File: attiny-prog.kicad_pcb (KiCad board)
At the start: 2 copper layers, 53.3 x 53.1 mm, 9 parts, among them J1 SOIC16_clip

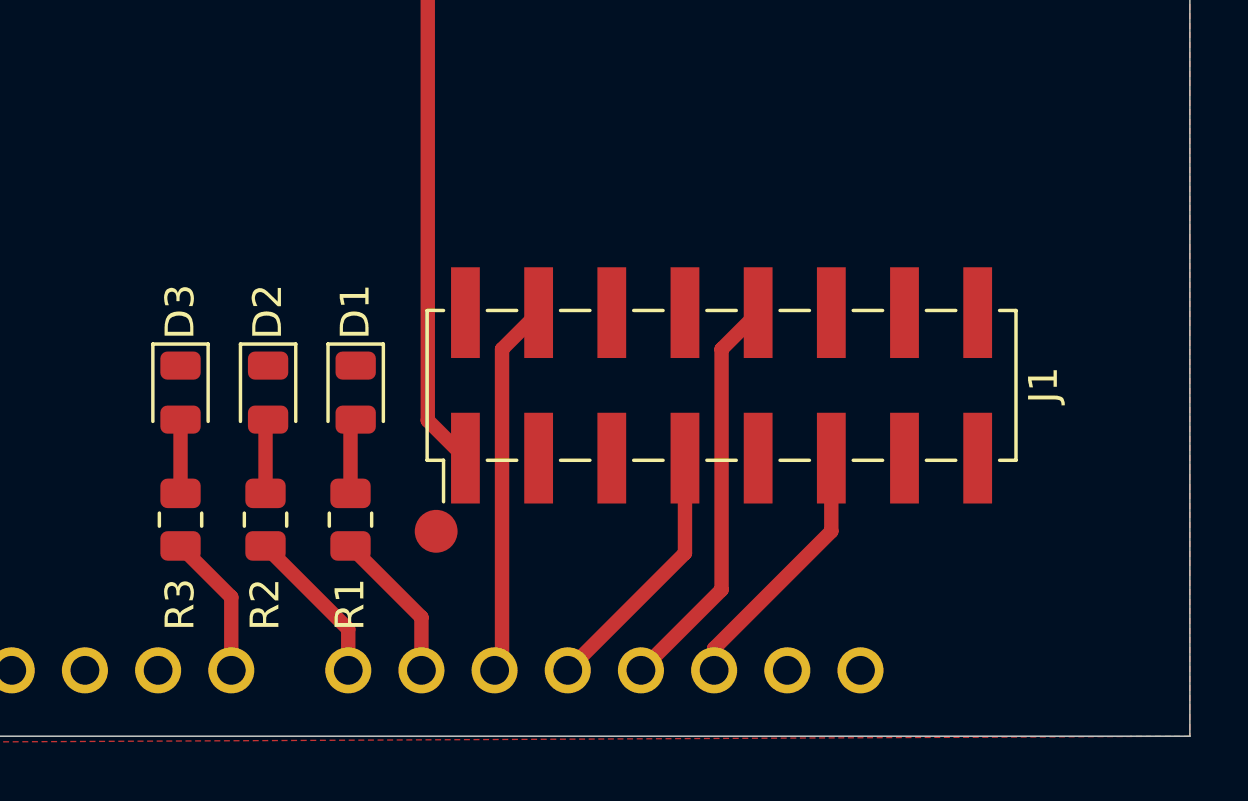
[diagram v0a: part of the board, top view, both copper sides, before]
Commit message: Second revision
* fixed SOIC_clip header pinout
* added reset capacitor value
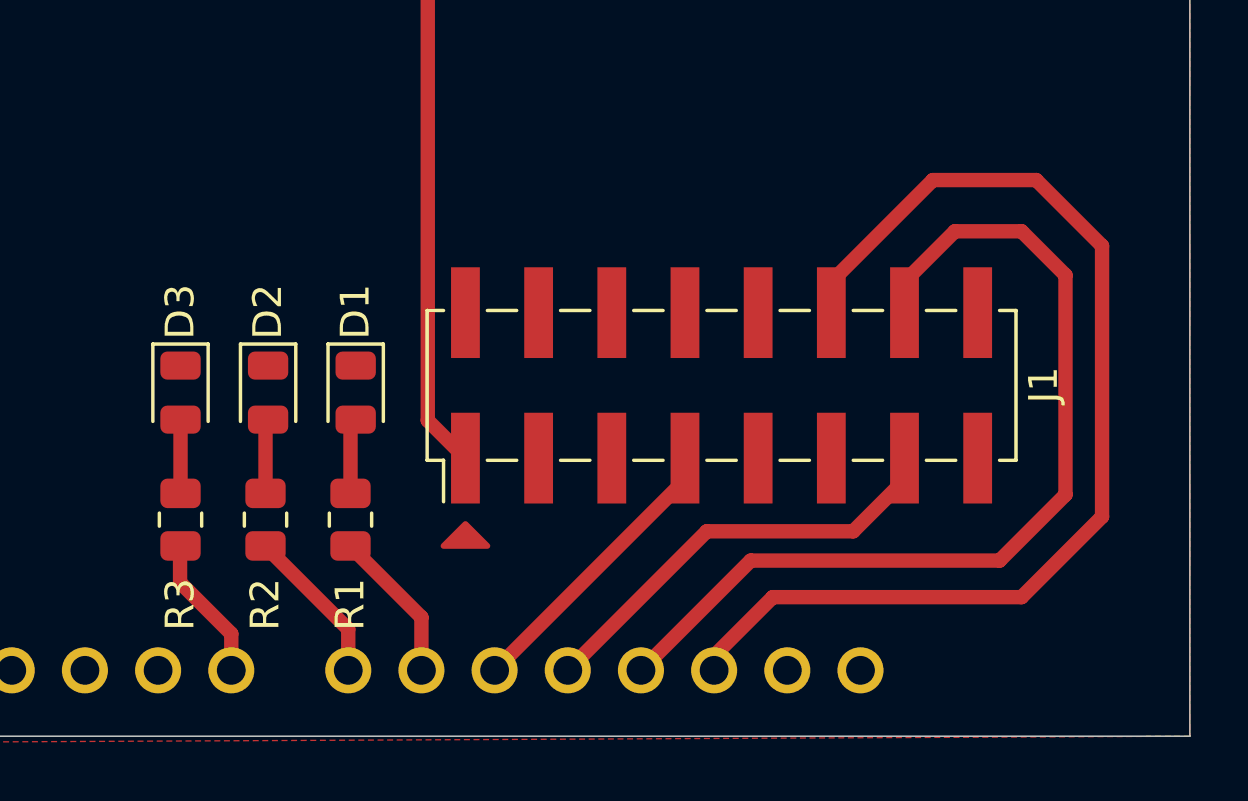
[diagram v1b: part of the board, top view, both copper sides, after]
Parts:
- C1: value C_Polarized -> 10u
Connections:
- J1 pad 10: MISO -> unconnected-(J1-Pin_10-Pad10)
- J1 pad 11: SCK -> unconnected-(J1-Pin_11-Pad11)
- J1 pad 12: unconnected-(J1-Pin_12-Pad12) -> SCK
- J1 pad 13: unconnected-(J1-Pin_13-Pad13) -> MOSI
- J1 pad 14: unconnected-(J1-Pin_14-Pad14) -> MISO
- J1 pad 16: GND -> unconnected-(J1-Pin_16-Pad16)
- J1 pad 2: unconnected-(J1-Pin_2-Pad2) -> GND
- J1 pad 4: tinyRESET -> unconnected-(J1-Pin_4-Pad4)
- J1 pad 7: MOSI -> tinyRESET
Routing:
- net SCK: track 9.05 -> 38.2 mm
- net MISO: track 14.1 -> 32.9 mm
- net MOSI: track 9.05 -> 15.2 mm
- net tinyRESET: track 13.0 -> 10.1 mm
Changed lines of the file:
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@@
 	(title_block
 		(title "ATTiny84A Programmer for Uno")
-		(date "2024-12-09")
-		(rev "rev1")
+		(date "2024-12-11")
+		(rev "rev2")
 		(company "SEM")
 		(comment 1 "ArduinoISP hat for Tiny84A & SOIC16 clip")
@@
 	(net 23 "MISO")
 	(net 24 "GND")
-	(net 25 "unconnected-(J1-Pin_14-Pad14)")
+	(net 25 "unconnected-(J1-Pin_4-Pad4)")
 	(net 26 "unconnected-(J1-Pin_3-Pad3)")
 	(net 27 "unconnected-(J1-Pin_9-Pad9)")
-	(net 28 "unconnected-(J1-Pin_12-Pad12)")
+	(net 28 "unconnected-(J1-Pin_16-Pad16)")
 	(net 29 "unconnected-(J1-Pin_8-Pad8)")
 	(net 30 "tinyVCC")
 	(net 31 "unconnected-(J1-Pin_15-Pad15)")
-	(net 32 "unconnected-(J1-Pin_13-Pad13)")
-	(net 33 "unconnected-(J1-Pin_2-Pad2)")
+	(net 32 "unconnected-(J1-Pin_10-Pad10)")
+	(net 33 "unconnected-(J1-Pin_11-Pad11)")
 	(net 34 "unconnected-(J1-Pin_6-Pad6)")
 	(net 35 "unconnected-(J1-Pin_5-Pad5)")
@@
 			)
 		)
-		(property "Value" "C_Polarized"
+		(property "Value" "10u"
 			(at 0 3.7 90)
 			(layer "F.Fab")
@@
 			)
 		)
-		(property "Description" "Generic connector, double row, 02x08, counter clockwise pin numbering scheme (similar to DIP package numbering), script generated (kicad-library-utils/schlib/autogen/connector/)"
+		(property "Description" "Generic connector, double row, 02x08, odd/even pin numbering scheme (row 1 odd numbers, row 2 even numbers), script generated (kicad-library-utils/schlib/autogen/connector/)"
 			(at 0 0 90)
 			(unlocked yes)
@@
 		)
 		(fp_text user "${REFERENCE}"
-			(at 0 0 360)
+			(at 0 0 0)
 			(layer "F.Fab")
 			(effects
@@
 			(size 3.15 1)
 			(layers "F.Cu" "F.Paste" "F.Mask")
-			(net 33 "unconnected-(J1-Pin_2-Pad2)")
+			(net 24 "GND")
 			(pinfunction "Pin_2")
 			(pintype "passive")
@@
 			(size 3.15 1)
 			(layers "F.Cu" "F.Paste" "F.Mask")
-			(net 4 "tinyRESET")
+			(net 25 "unconnected-(J1-Pin_4-Pad4)")
 			(pinfunction "Pin_4")
 			(pintype "passive")
@@
 			(size 3.15 1)
 			(layers "F.Cu" "F.Paste" "F.Mask")
-			(net 8 "MOSI")
+			(net 4 "tinyRESET")
 			(pinfunction "Pin_7")
 			(pintype "passive")
@@
 			(net 29 "unconnected-(J1-Pin_8-Pad8)")
 			(pinfunction "Pin_8")
-			(pintype "passive+no_connect")
+			(pintype "passive")
 		)
 		(pad "9" smd rect
@@
 			(net 27 "unconnected-(J1-Pin_9-Pad9)")
 			(pinfunction "Pin_9")
-			(pintype "passive+no_connect")
+			(pintype "passive")
 		)
 		(pad "10" smd rect
@@
 			(size 3.15 1)
 			(layers "F.Cu" "F.Paste" "F.Mask")
-			(net 23 "MISO")
+			(net 32 "unconnected-(J1-Pin_10-Pad10)")
 			(pinfunction "Pin_10")
 			(pintype "passive")
@@
 			(size 3.15 1)
 			(layers "F.Cu" "F.Paste" "F.Mask")
-			(net 14 "SCK")
+			(net 33 "unconnected-(J1-Pin_11-Pad11)")
 			(pinfunction "Pin_11")
 			(pintype "passive")
@@
 			(size 3.15 1)
 			(layers "F.Cu" "F.Paste" "F.Mask")
-			(net 28 "unconnected-(J1-Pin_12-Pad12)")
+			(net 14 "SCK")
 			(pinfunction "Pin_12")
 			(pintype "passive")
@@
 			(size 3.15 1)
 			(layers "F.Cu" "F.Paste" "F.Mask")
-			(net 32 "unconnected-(J1-Pin_13-Pad13)")
+			(net 8 "MOSI")
 			(pinfunction "Pin_13")
 			(pintype "passive")
@@
 			(size 3.15 1)
 			(layers "F.Cu" "F.Paste" "F.Mask")
-			(net 25 "unconnected-(J1-Pin_14-Pad14)")
+			(net 23 "MISO")
 			(pinfunction "Pin_14")
 			(pintype "passive")
@@
 			(net 31 "unconnected-(J1-Pin_15-Pad15)")
 			(pinfunction "Pin_15")
-			(pintype "passive")
+			(pintype "passive+no_connect")
 		)
 		(pad "16" smd rect
@@
 			(size 3.15 1)
 			(layers "F.Cu" "F.Paste" "F.Mask")
-			(net 24 "GND")
+			(net 28 "unconnected-(J1-Pin_16-Pad16)")
 			(pinfunction "Pin_16")
-			(pintype "passive")
+			(pintype "passive+no_connect")
 		)
 		(model "${KICAD8_3DMODEL_DIR}/Connector_PinHeader_2.54mm.3dshapes/PinHeader_2x08_P2.54mm_Vertical_SMD.wrl"
@@
 		(tags "Arduino UNO R2")
 		(property "Reference" "A1"
-			(at 1.27 3.81 360)
+			(at 1.27 3.81 0)
 			(layer "B.SilkS")
 			(effects
@@
 		)
 		(fp_text user "${REFERENCE}"
-			(at 0 -19.05 360)
+			(at 0 -19.05 0)
 			(layer "B.Fab")
 			(effects
@@
 		)
 	)
-	(gr_circle
-		(center 150.622 112.522)
-		(end 151.34042 112.522)
+	(gr_poly
+		(pts
+			(xy 150.876 113.03) (xy 151.638 112.268) (xy 152.4 113.03)
+		)
 		(stroke
-			(width 0.05)
+			(width 0.2)
 			(type solid)
 		)
@@
 	(gr_text "ATTiny24A/44A/84A\nProgrammer for Uno\n\n2024 CsokiCraft"
 		(at 136.652 82.296 0)
-		(layer "F.Cu")
+		(layer "F.Cu" knockout)
 		(effects
 			(font
@@
 	)
 	(segment
-		(start 152.908 106.202)
-		(end 152.908 117.09)
+		(start 152.65 117.348)
+		(end 159.258 110.74)
 		(width 0.5)
 		(layer "F.Cu")
@@
 	)
 	(segment
-		(start 154.178 104.932)
-		(end 152.908 106.202)
+		(start 159.258 110.74)
+		(end 159.258 109.982)
 		(width 0.5)
 		(layer "F.Cu")
@@
 	)
 	(segment
-		(start 152.908 117.09)
-		(end 152.65 117.348)
+		(start 156.21 69.088)
+		(end 156.21 71.968)
 		(width 0.5)
 		(layer "F.Cu")
-		(net 4)
+		(net 7)
 	)
 	(segment
-		(start 156.21 69.088)
-		(end 156.21 71.968)
+		(start 160.016 112.522)
+		(end 165.1 112.522)
 		(width 0.5)
 		(layer "F.Cu")
-		(net 7)
+		(net 8)
+	)
+	(segment
+		(start 165.1 112.522)
+		(end 166.878 110.744)
+		(width 0.5)
+		(layer "F.Cu")
+		(net 8)
 	)
 	(segment
-		(start 159.258 113.28)
-		(end 155.19 117.348)
+		(start 166.878 110.744)
+		(end 166.878 109.982)
 		(width 0.5)
 		(layer "F.Cu")
@@
 	)
 	(segment
-		(start 159.258 109.982)
-		(end 159.258 113.28)
+		(start 155.19 117.348)
+		(end 160.016 112.522)
 		(width 0.5)
 		(layer "F.Cu")
@@
 	)
 	(segment
-		(start 160.27 116.59)
-		(end 160.27 117.348)
+		(start 167.865 100.33)
+		(end 164.338 103.857)
+		(width 0.5)
+		(layer "F.Cu")
+		(net 14)
+	)
+	(segment
+		(start 160.27 116.844)
+		(end 162.306 114.808)
+		(width 0.5)
+		(layer "F.Cu")
+		(net 14)
+	)
+	(segment
+		(start 160.27 117.348)
+		(end 160.27 116.844)
 		(width 0.5)
 		(layer "F.Cu")
@@
 	)
 	(segment
-		(start 164.338 112.522)
-		(end 160.27 116.59)
+		(start 171.45 100.33)
+		(end 167.865 100.33)
 		(width 0.5)
 		(layer "F.Cu")
@@
 	)
 	(segment
-		(start 164.338 109.982)
-		(end 164.338 112.522)
+		(start 173.736 102.616)
+		(end 171.45 100.33)
 		(width 0.5)
 		(layer "F.Cu")
@@
 	)
 	(segment
-		(start 160.528 106.202)
-		(end 161.798 104.932)
+		(start 173.736 112.014)
+		(end 173.736 102.616)
+		(width 0.5)
+		(layer "F.Cu")
+		(net 14)
+	)
+	(segment
+		(start 162.306 114.808)
+		(end 170.942 114.808)
+		(width 0.5)
+		(layer "F.Cu")
+		(net 14)
+	)
+	(segment
+		(start 164.338 103.857)
+		(end 164.338 104.932)
+		(width 0.5)
+		(layer "F.Cu")
+		(net 14)
+	)
+	(segment
+		(start 170.942 114.808)
+		(end 173.736 112.014)
+		(width 0.5)
+		(layer "F.Cu")
+		(net 14)
+	)
+	(segment
+		(start 166.878 103.857)
+		(end 168.627 102.108)
+		(width 0.5)
+		(layer "F.Cu")
+		(net 23)
+	)
+	(segment
+		(start 170.18 113.538)
+		(end 161.54 113.538)
+		(width 0.5)
+		(layer "F.Cu")
+		(net 23)
+	)
+	(segment
+		(start 172.466 111.252)
+		(end 170.18 113.538)
+		(width 0.5)
+		(layer "F.Cu")
+		(net 23)
+	)
+	(segment
+		(start 168.627 102.108)
+		(end 170.942 102.108)
+		(width 0.5)
+		(layer "F.Cu")
+		(net 23)
+	)
+	(segment
+		(start 161.54 113.538)
+		(end 157.73 117.348)
 		(width 0.5)
 		(layer "F.Cu")
@@
 	)
 	(segment
-		(start 157.73 117.348)
-		(end 160.528 114.55)
+		(start 166.878 104.932)
+		(end 166.878 103.857)
 		(width 0.5)
 		(layer "F.Cu")
@@
 	)
 	(segment
-		(start 160.528 114.55)
-		(end 160.528 106.202)
+		(start 172.466 103.632)
+		(end 172.466 111.252)
+		(width 0.5)
+		(layer "F.Cu")
+		(net 23)
+	)
+	(segment
+		(start 170.942 102.108)
+		(end 172.466 103.632)
 		(width 0.5)
 		(layer "F.Cu")
@@
 	)
 	(segment
-		(start 143.51 117.348)
-		(end 143.51 114.808)
+		(start 143.51 116.078)
+		(end 141.732 114.3)
 		(width 0.5)
 		(layer "F.Cu")
@@
 	)
 	(segment
-		(start 143.51 114.808)
+		(start 141.732 114.3)
 		(end 141.732 113.03)
 		(width 0.5)
 		(layer "F.Cu")
+		(net 38)
+	)
+	(segment
+		(start 143.51 117.348)
+		(end 143.51 116.078)
+		(width 0.5)
+		(layer "F.Cu")
